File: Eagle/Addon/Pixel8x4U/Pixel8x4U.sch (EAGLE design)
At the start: 28 parts, among them J1 5V, J2 I2C, J3 RJ45, J4 RJ45, J5 GPIOC, Q1 DIODES_INC._DMG2305UX-13DIODE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, Q2 DMMT5401-7-F_0_0, U1 74HCT245

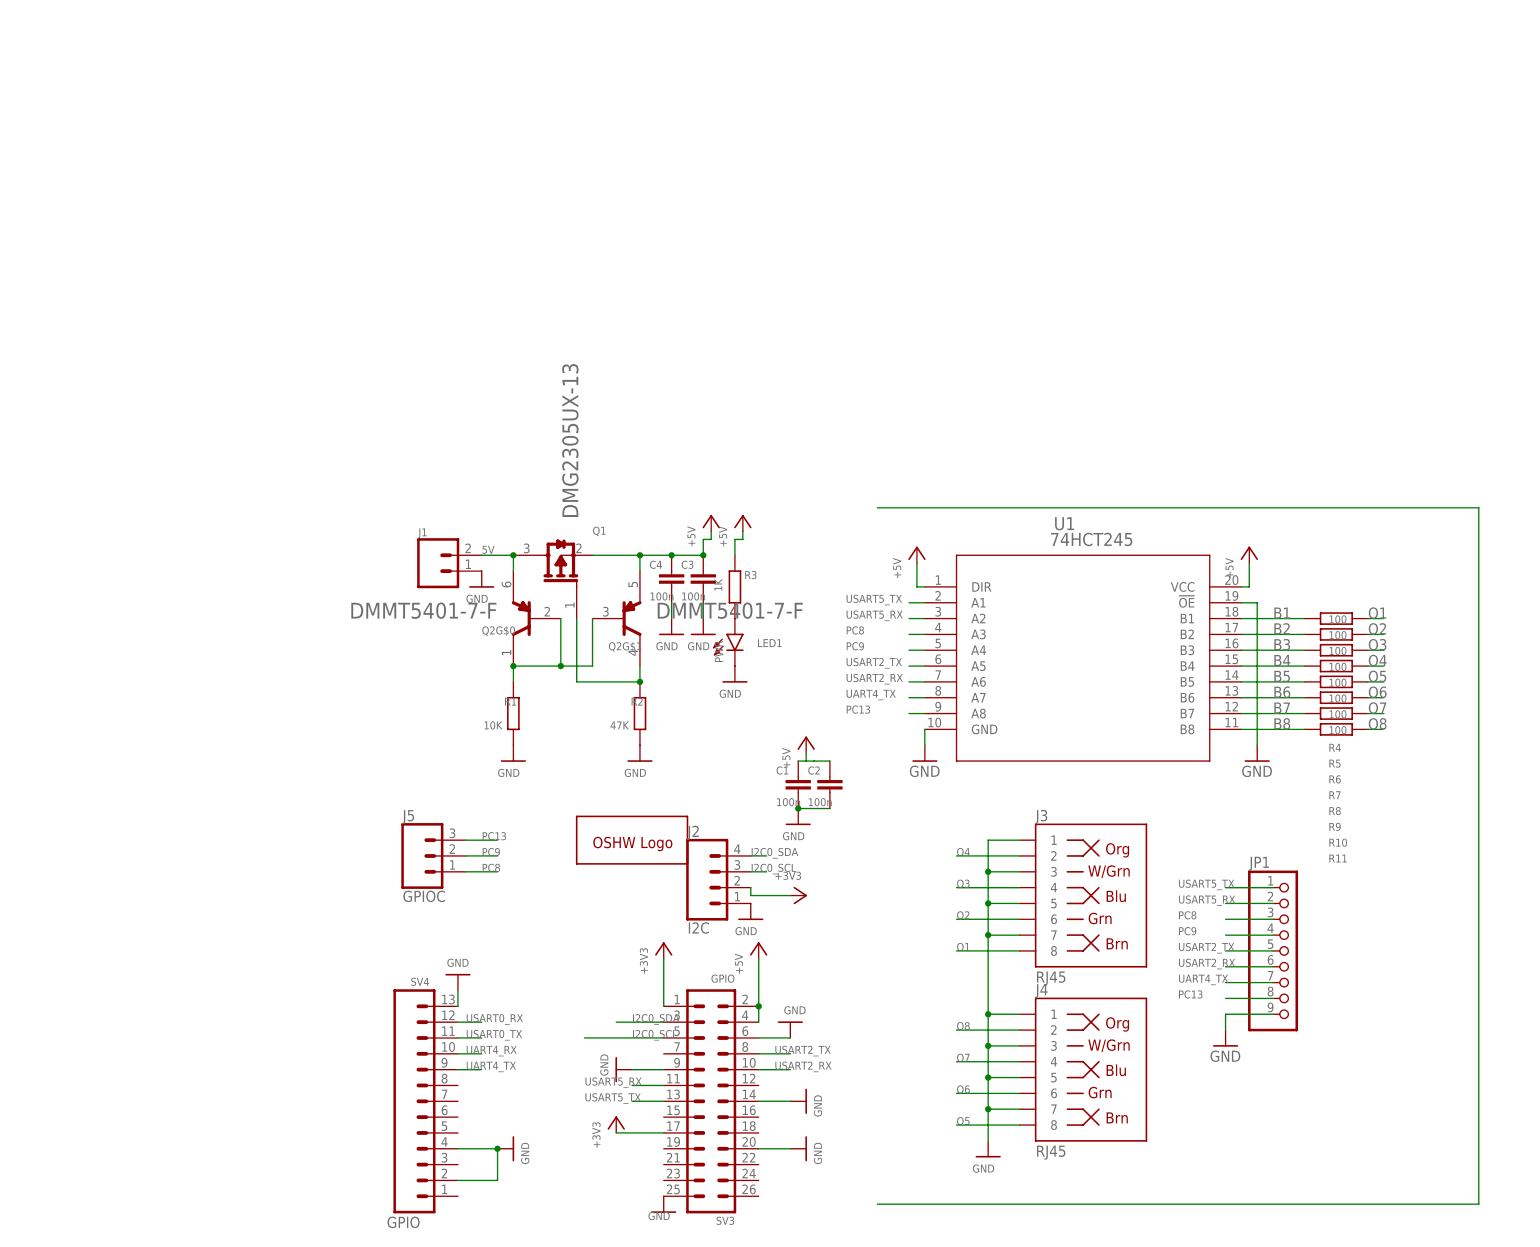
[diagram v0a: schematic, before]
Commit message: Updated Add-on Pixel 8x 4 Universes
*. Added support for clock based led chip's (for example APA102)
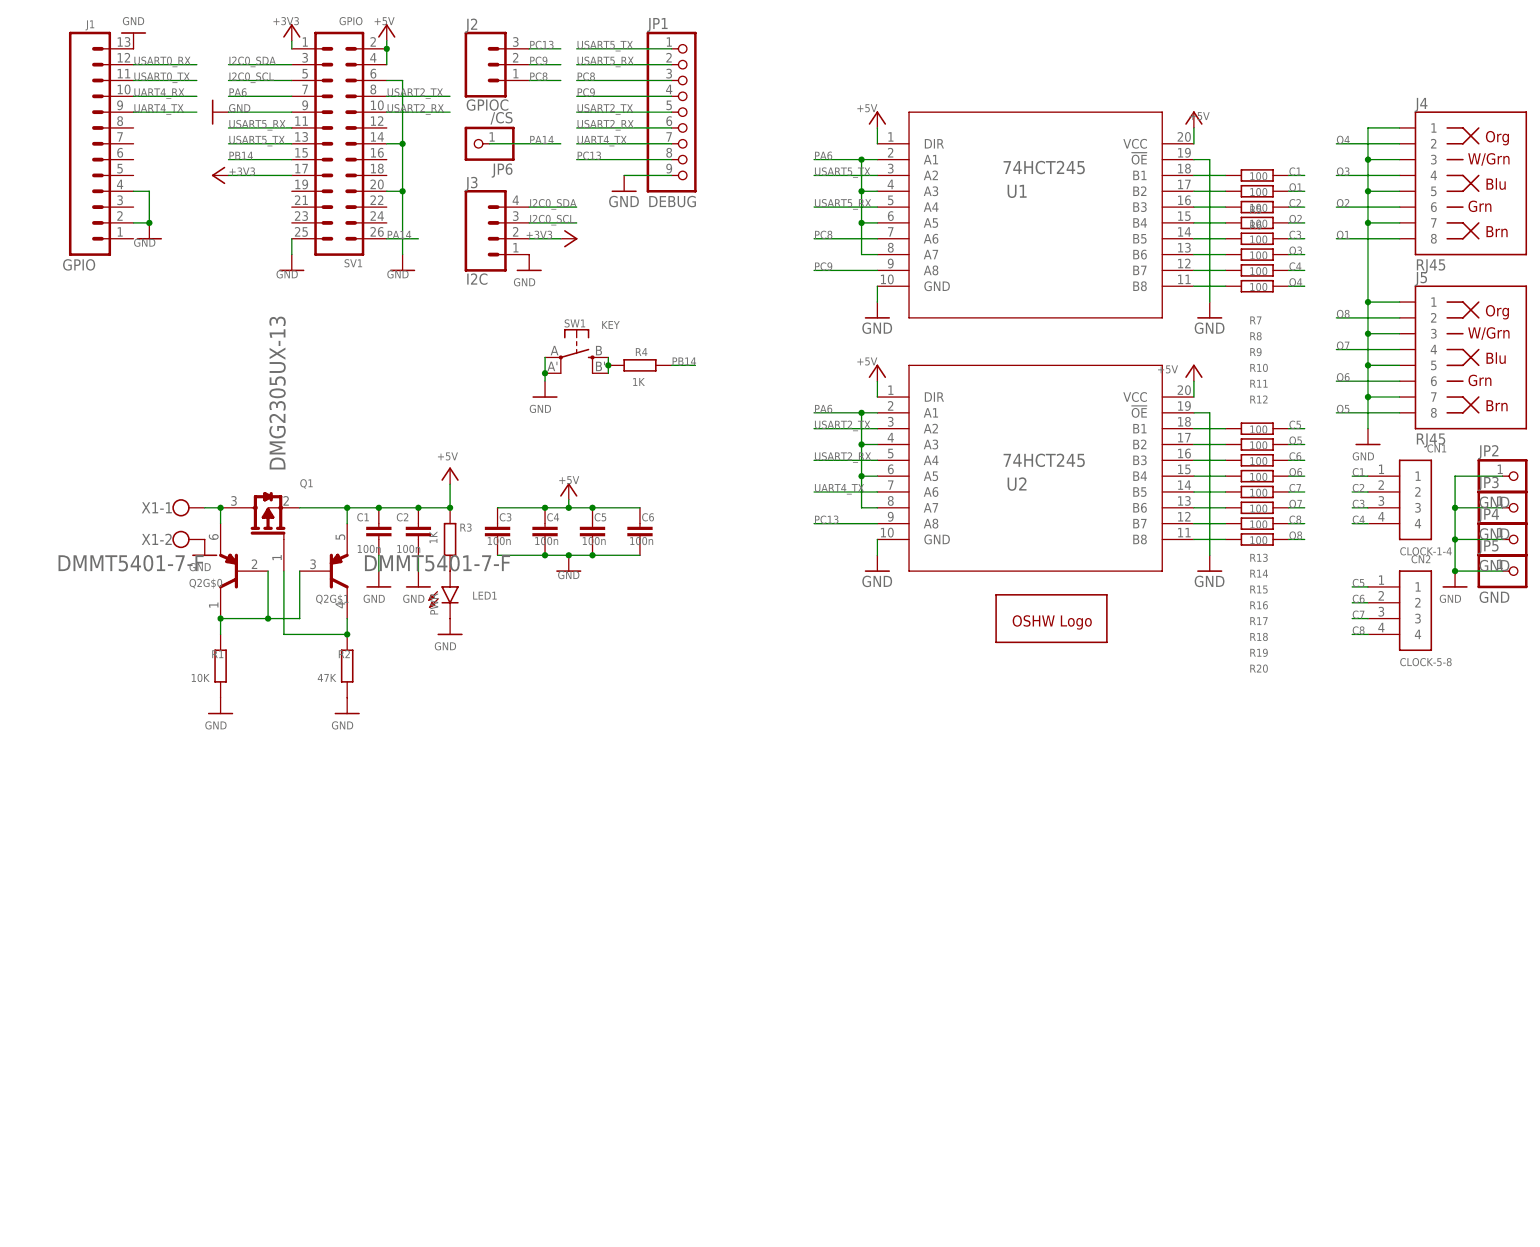
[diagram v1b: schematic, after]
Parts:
- removed SV3: GPIO, con-lstb:MA13-2
- removed SV4: GPIO, SparkFun-Connectors:CONN_13
- added C5, C6: 100n, rcl:C-EUC0603
- added CN1: CLOCK-1-4, adafruit:1X4-CLEANBIG
- added CN2: CLOCK-5-8, adafruit:1X4-CLEANBIG
- added JP2, JP3, JP4, JP5: GND, adafruit:PINHD-1X1CB
- added JP6: /CS, adafruit:PINHD-1X1CB
- added R12, R13, R14, R15, R16, R17, R18, R19, R20: 100, rcl:R-EU_R0402
- added SV1: GPIO, con-lstb:MA13-2
- added SW1: KEY, adafruit:SPST_TACT-EVQQ2
- added U2: 74HCT245, SN74HCT245PWR:SN74HCT245PWR
- added X1: (no value), con-wago-500:W237-102
- J1: value 5V -> GPIO; device SparkFun-Connectors:CONN_023.5MM -> SparkFun-Connectors:CONN_13
- J2: value I2C -> GPIOC; device SparkFun-Connectors:CONN_04 -> SparkFun-Connectors:CONN_03
- J3: value RJ45 -> I2C; device SparkFun-Connectors:RJ45-8 -> SparkFun-Connectors:CONN_04
- J5: value GPIOC -> RJ45; device SparkFun-Connectors:CONN_03 -> SparkFun-Connectors:RJ45-8
- JP1: value (none) -> DEBUG
- R4: value 100 -> 1K; device rcl:R-EU_R0402 -> resistor:R-EU_R0402
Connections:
- removed net B1: R4.1, U1.B1
- removed net B2: R5.1, U1.B2
- removed net B3: R6.1, U1.B3
- removed net B4: R7.1, U1.B4
- removed net B5: R8.1, U1.B5
- removed net B6: R9.1, U1.B6
- removed net B7: R10.1, U1.B7
- removed net B8: R11.1, U1.B8
- new net C1: CN1.1, R5.2
- new net C2: CN1.2, R7.2
- new net C3: CN1.3, R9.2
- new net C4: CN1.4, R11.2
- new net C5: CN2.1, R13.2
- new net C6: CN2.2, R15.2
- new net C7: CN2.3, R17.2
- new net C8: CN2.4, R19.2
- new net N$10: R7.1, U1.B3
- new net N$11: R14.1, U2.B2
- new net N$12: R16.1, U2.B4
- new net N$13: R18.1, U2.B6
- new net N$15: R20.1, U2.B8
- new net N$16: R9.1, U1.B5
- new net N$17: R11.1, U1.B7
- new net N$18: R13.1, U2.B1
- new net N$19: R15.1, U2.B3
- new net N$20: R17.1, U2.B5
- new net N$21: R19.1, U2.B7
- new net N$4: R4.1, SW1.S, SW1.S1
- new net N$5: R6.1, U1.B2
- new net N$6: R12.1, U1.B8
- new net N$7: R10.1, U1.B6
- new net N$8: R8.1, U1.B4
- new net N$9: R5.1, U1.B1
- new net PA14: JP6.1, SV1.26
- new net PA6: SV1.7, U1.A1, U1.A3, U1.A5, U1.A7, U2.A1, U2.A3, U2.A5, U2.A7
- new net PB14: R4.2, SV1.15
- net +3V3: now also J3.2, SV1.1, SV1.17; no longer J2.2, SV3.1, SV3.17
- net +5V: now also C5.1, C6.1, SV1.2, SV1.4, U2.DIR, U2.VCC; no longer SV3.2, SV3.4
- net GND: now also C5.2, C6.2, J1.13, J1.2, J1.4, J5.1, J5.3, J5.5, J5.7, JP2.1, JP3.1, JP4.1, JP5.1, SV1.14, SV1.20, SV1.25, SV1.6, SV1.9, SW1.P, SW1.P1, U2.!OE, U2.GND, X1-2.KL; no longer J1.1, J2.1, J3.3, J3.5, J3.7, SV3.14, SV3.20, SV3.25, SV3.6, SV3.9, SV4.13, SV4.2, SV4.4
- net I2C0_SCL: now also J3.3, SV1.5; no longer J2.3, SV3.5
- net I2C0_SDA: now also J3.4, SV1.3; no longer J2.4, SV3.3
- net N$2: now also X1-1.KL; no longer J1.2
- net O1: now also J4.8, R6.2; no longer J3.8, R4.2
- net O2: now also J4.6, R8.2; no longer J3.6, R5.2
- net O3: now also J4.4, R10.2; no longer J3.4, R6.2
- net O4: now also J4.2, R12.2; no longer J3.2, R7.2
- net O5: now also J5.8, R14.2; no longer J4.8, R8.2
- net O6: now also J5.6, R16.2; no longer J4.6, R9.2
- net O7: now also J5.4, R18.2; no longer J4.4, R10.2
- net O8: now also J5.2, R20.2; no longer J4.2, R11.2
- net PC13: now also J2.3, U2.A8; no longer J5.3, U1.A8
- net PC8: now also J2.1, U1.A6; no longer J5.1, U1.A3
- net PC9: now also J2.2, U1.A8; no longer J5.2, U1.A4
- net UART4_RX: now also J1.10; no longer SV4.10
- net UART4_TX: now also J1.9, U2.A6; no longer SV4.9, U1.A7
- net USART0_RX: now also J1.12; no longer SV4.12
- net USART0_TX: now also J1.11; no longer SV4.11
- net USART2_RX: now also SV1.10, U2.A4; no longer SV3.10, U1.A6
- net USART2_TX: now also SV1.8, U2.A2; no longer SV3.8, U1.A5
- net USART5_RX: now also SV1.11, U1.A4; no longer SV3.11, U1.A2
- net USART5_TX: now also SV1.13, U1.A2; no longer SV3.13, U1.A1
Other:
- moved on the sheet: C1, C2, C3, C4, J4, JP1, LED1, Q1, Q2G$0, Q2G$1, R1, R10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
